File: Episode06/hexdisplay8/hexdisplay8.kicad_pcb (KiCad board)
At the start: 2 copper layers, 18 parts, among them J1 Conn_02x05_Counter_Clockwise, J2 Conn_02x05_Counter_Clockwise, J3 Conn_01x02, J4 Conn_01x08, J5 Conn_01x06, Q1 MMBT3906, Q2 MMBT3906, U1 ATTINY2313A-SU

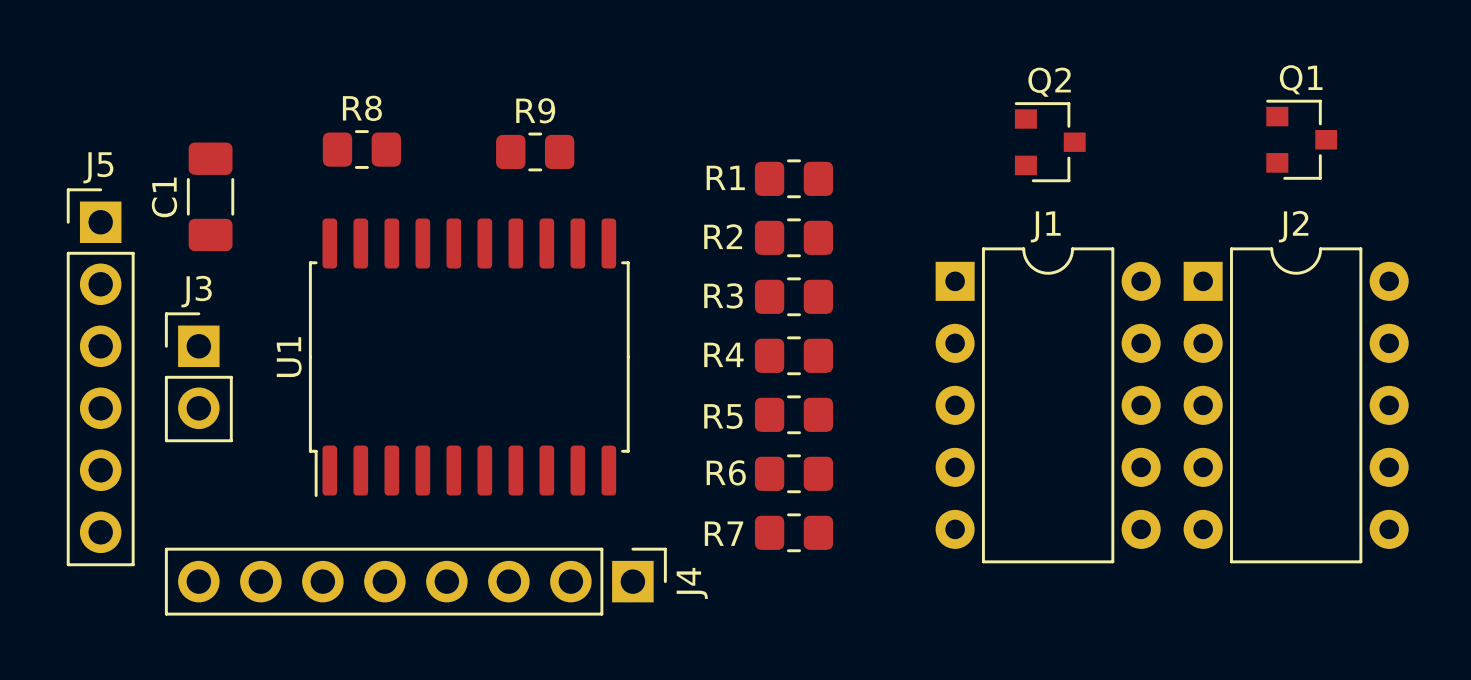
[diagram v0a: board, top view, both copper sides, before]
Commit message: routed signals
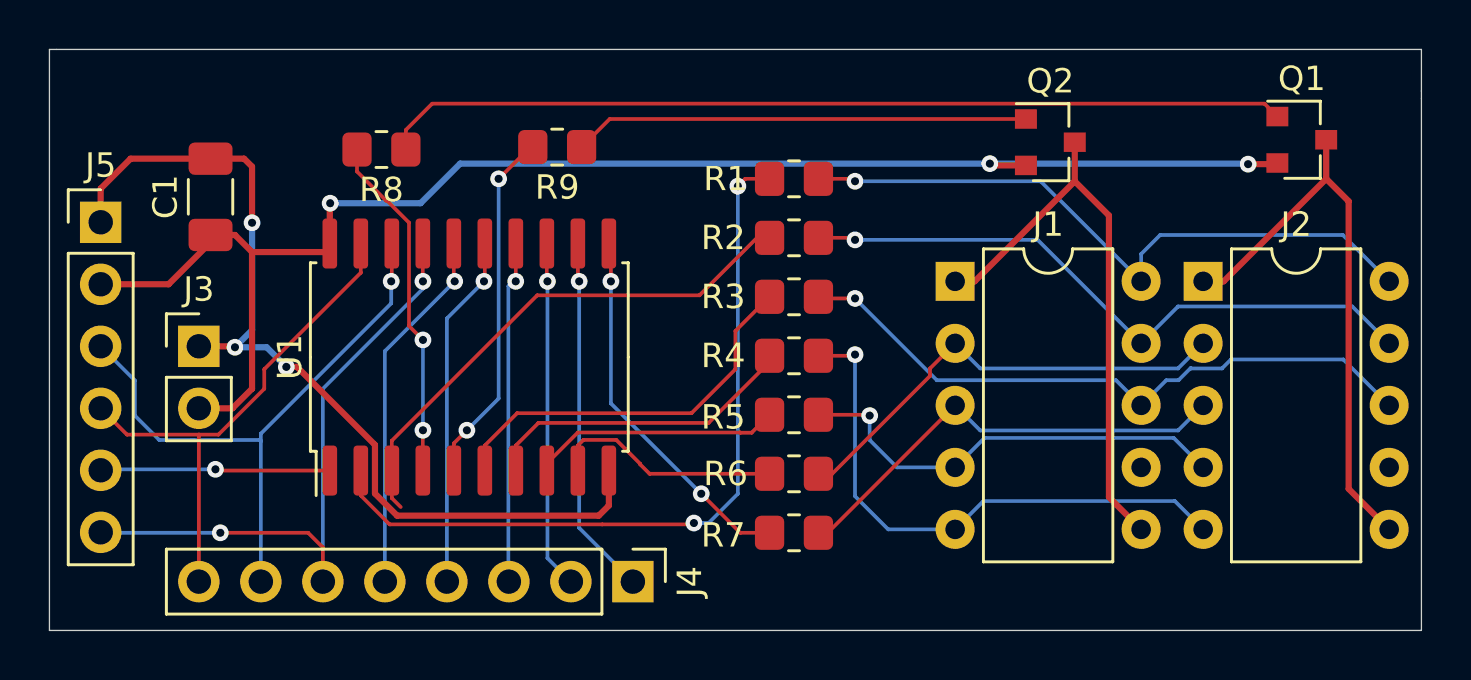
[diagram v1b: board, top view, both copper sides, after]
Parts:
- moved R9 0.92 mm to (156.9, 102.2), turned to 180 degrees
- moved R8 0.80 mm to (149.7, 102.3), turned to 180 degrees
- turned R7 to 180 degrees
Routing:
- net VCC: track 0.00 -> 61.7 mm, vias 0 -> 3
- net GND: track 0.00 -> 38.4 mm, vias 0 -> 3
- net Net-(Q1-Pad1): track 0.00 -> 37.2 mm
- net Net-(R1-Pad2): track 0.00 -> 31.5 mm, vias 0 -> 2
- net /A: track 0.00 -> 27.3 mm, vias 0 -> 1
- net /C: track 0.00 -> 26.8 mm, vias 0 -> 1
- net /B: track 0.00 -> 26.4 mm, vias 0 -> 1
- net /D5: track 0.00 -> 26.3 mm, vias 0 -> 2
- net /D6: track 0.00 -> 25.3 mm, vias 0 -> 1
- net /CA1: track 0.00 -> 23.8 mm
- net /CA2: track 0.00 -> 23.6 mm
- net /D: track 0.00 -> 23.1 mm, vias 0 -> 1
- net Net-(R2-Pad2): track 0.00 -> 21.8 mm
- net /D7: track 0.00 -> 21.5 mm
- net /F: track 0.00 -> 19.0 mm
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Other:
- board outline added: 56.2 x 23.8 mm

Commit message: added additional silkscreen markings
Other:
- board text added: "(c) 2021 daveho hacks"
- board text added: "D0"
- board text added: "D7"
- board text added: "https://github.com/daveho/RandomStuff/tree/master/ Episode06/hexdisplay8"
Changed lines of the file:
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@@
   (general
     (thickness 1.6)
-    (drawings 7)
+    (drawings 11)
     (tracks 267)
     (zones 0)
@@
     )
   )
+  (gr_text D0 (at 160.1 118.1) (layer F.SilkS)
+    (effects (font (size 0.75 0.75) (thickness 0.15)))
+  )
+  (gr_text D7 (at 142.3 118.1) (layer F.SilkS)
+    (effects (font (size 0.75 0.75) (thickness 0.15)))
+  )
+  (gr_text "https://github.com/daveho/RandomStuff/tree/master/\n  Episode06/hexdisplay8" (at 137 99.9) (layer F.SilkS)
+    (effects (font (size 0.75 0.75) (thickness 0.15)) (justify left))
+  )
+  (gr_text "(c) 2021 daveho hacks" (at 172 120.5) (layer F.SilkS)
+    (effects (font (size 1 1) (thickness 0.15)))
+  )
   (gr_line (start 136.1 122) (end 192.3 122) (layer Edge.Cuts) (width 0.05))

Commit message: added ground planes
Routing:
- added copper zone on B.Cu, net GND
- added copper zone on F.Cu, net GND
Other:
- board text added: "GND"
- board text added: "MISO"
- board text added: "MOSI"
- board text added: "RST"
- board text added: "SCK"
- board text added: "VCC"
